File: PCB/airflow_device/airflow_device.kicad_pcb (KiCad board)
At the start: 2 copper layers, 2 parts, among them J1 GRID_EYE Connector, U1 esp32-wemos-d1-mini

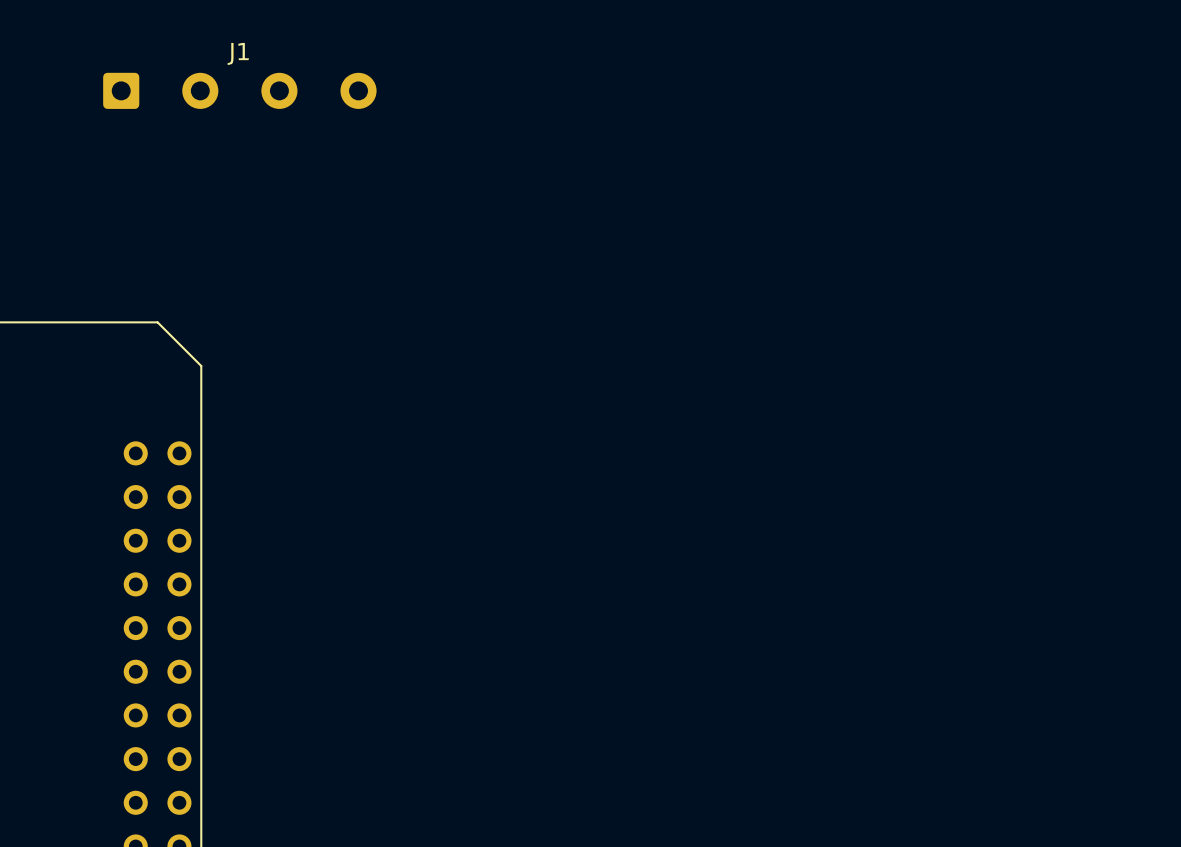
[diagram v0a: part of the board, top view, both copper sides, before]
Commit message: Adding more components, and fixing footprints
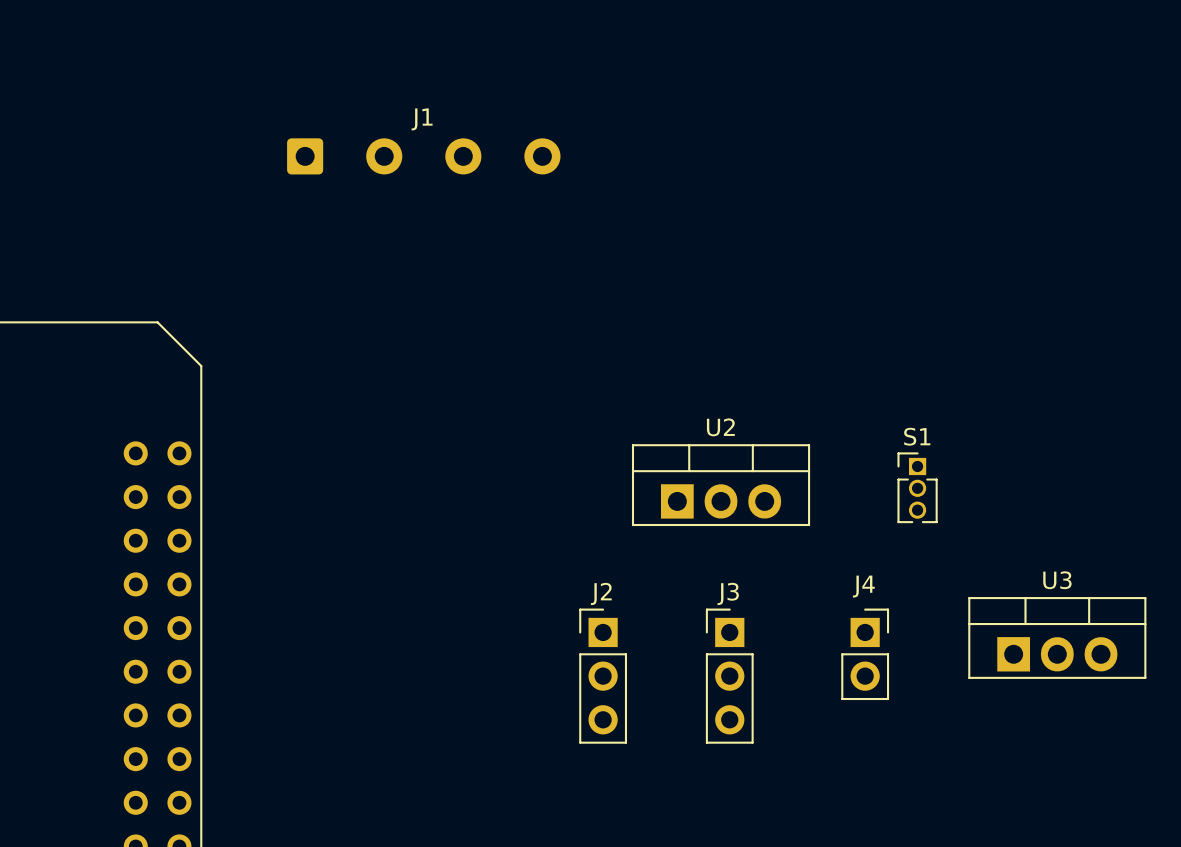
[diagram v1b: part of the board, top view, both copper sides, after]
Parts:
- added J2: Grideye Servo, Connector_PinHeader_2.54mm:PinHeader_1x03_P2.54mm_Vertical, F.Cu at (155.4, 88.9)
- added J3: Vent Servo, Connector_PinHeader_2.54mm:PinHeader_1x03_P2.54mm_Vertical, F.Cu at (162.8, 88.9)
- added J4: Conn_01x02_Pin, Connector_PinSocket_2.54mm:PinSocket_1x02_P2.54mm_Vertical, F.Cu at (170.7, 88.9)
- added S1: Toggle Switch, Connector_PinHeader_1.27mm:PinHeader_1x03_P1.27mm_Vertical, F.Cu at (173.7, 79.2)
- added U2: 3v3 regulator, Package_TO_SOT_THT:TO-220-3_Vertical, F.Cu at (159.8, 81.3)
- added U3: LM2940, Package_TO_SOT_THT:TO-220-3_Vertical, F.Cu at (179.3, 90.2)
- moved J1 11.4 mm to (138.1, 61.2)
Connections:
- J1 pad 1: unconnected-(J1-GND-Pad1) -> GND
- J1 pad 2: unconnected-(J1-SDA-Pad2) -> Net-(J1-SDA)
- J1 pad 3: unconnected-(J1-SCL-Pad3) -> Net-(J1-SCL)
- J1 pad 4: unconnected-(J1-Vin-Pad4) -> /3v3
- U1 pad 1: unconnected-(U1-GND-Pad1) -> GND
- U1 pad 16: unconnected-(U1-3V3-Pad16) -> /3v3
- U1 pad 22: unconnected-(U1-GND-Pad22) -> GND
- U1 pad 25: unconnected-(U1-IO_22/D1/SCL-Pad25) -> Net-(J1-SCL)
- U1 pad 27: unconnected-(U1-IO_21/D2/SDA-Pad27) -> Net-(J1-SDA)
- U1 pad 33: unconnected-(U1-GND-Pad33) -> GND
- U1 pad 34: unconnected-(U1-IO_00-Pad34) -> Net-(J3-SIG)
- U1 pad 36: unconnected-(U1-IO_02-Pad36) -> Net-(J2-SIG)

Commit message: Likely Functional PCB
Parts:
- removed S1: Toggle Switch, Connector_PinHeader_1.27mm:PinHeader_1x03_P1.27mm_Vertical
- added C2: 0.47uF, Capacitor_SMD:C_0805_2012Metric_Pad1.18x1.45mm_HandSolder, F.Cu at (104.6, 101.1)
- added C3: 22uF, Capacitor_SMD:C_0805_2012Metric_Pad1.18x1.45mm_HandSolder, F.Cu at (110.9, 101.1)
- added C4: .1uF, Capacitor_SMD:C_0805_2012Metric_Pad1.18x1.45mm_HandSolder, F.Cu at (95.7, 101.1)
- added C5: 10uF, Capacitor_SMD:C_0805_2012Metric_Pad1.18x1.45mm_HandSolder, F.Cu at (89.6, 101.1)
- added D1: Tracking LED, LED_THT:LED_D3.0mm, F.Cu at (85.1, 106.3)
- added D2: LED, LED_THT:LED_D3.0mm, F.Cu at (93.0, 106.3)
- added D3: LED, LED_THT:LED_D3.0mm, F.Cu at (77.0, 106.3)
- added R1: 4.7k, Resistor_SMD:R_0805_2012Metric_Pad1.20x1.40mm_HandSolder, F.Cu at (86.4, 109.6)
- added R2: 4.7k, Resistor_SMD:R_0805_2012Metric_Pad1.20x1.40mm_HandSolder, F.Cu at (100.3, 72.1)
- added R3: 4.7k, Resistor_SMD:R_0805_2012Metric_Pad1.20x1.40mm_HandSolder, F.Cu at (100.3, 77.2)
- added R4: 4.7k, Resistor_SMD:R_0805_2012Metric_Pad1.20x1.40mm_HandSolder, F.Cu at (94.0, 109.6)
- added R5: 4.7k, Resistor_SMD:R_0805_2012Metric_Pad1.20x1.40mm_HandSolder, F.Cu at (78.2, 109.6)
- added R6: 4.7k, Resistor_SMD:R_0805_2012Metric_Pad1.20x1.40mm_HandSolder, F.Cu at (78.0, 92.5)
- added R7: 4.7k, Resistor_SMD:R_0805_2012Metric_Pad1.20x1.40mm_HandSolder, F.Cu at (83.0, 79.5)
- added SW1: TOGGLE, Connector_PinHeader_2.54mm:PinHeader_1x03_P2.54mm_Vertical, F.Cu at (78.0, 96.5)
- added SW2: LEFT, Button_Switch_THT:SW_PUSH_6mm_H5mm, F.Cu at (88.4, 72.6)
- added SW3: RIGHT, Button_Switch_THT:SW_PUSH_6mm_H5mm, F.Cu at (104.5, 72.7)
- added SW4: XTRA, Button_Switch_THT:SW_PUSH_6mm_H5mm, F.Cu at (77.8, 72.2)
- J1: footprint Connector_Wire:SolderWire-0.5sqmm_1x04_P4.6mm_D0.9mm_OD2.1mm -> Connector_PinHeader_2.54mm:PinHeader_1x04_P2.54mm_Vertical
- moved U3 74.7 mm to (105.1, 98.6)
- moved U2 72.0 mm to (89.9, 98.6)
- moved J4 66.5 mm to (106.9, 107.7), turned to -90 degrees
- moved J1 24.9 mm to (147.3, 84.3), turned to 180 degrees
- moved J2 20.7 mm to (147.3, 107.9), turned to 180 degrees
- moved J3 16.6 mm to (147.3, 94.7), turned to 180 degrees
- moved U1 12.5 mm to (129.0, 92.7)
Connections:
- net Net-(J1-SCL) renamed /SCL
- net Net-(J1-SDA) renamed /SDA
- U1 pad 10: unconnected-(U1-IO_19/D6-Pad10) -> Net-(U1-IO_19/D6)
- U1 pad 12: unconnected-(U1-IO_23/D7-Pad12) -> Net-(U1-IO_23/D7)
- U1 pad 14: unconnected-(U1-IO_05/D8-Pad14) -> Net-(U1-IO_05/D8)
- U1 pad 29: unconnected-(U1-IO_17/D3-Pad29) -> Net-(U1-IO_17/D3)
- U1 pad 31: unconnected-(U1-IO_16/D4-Pad31) -> Net-(U1-IO_16/D4)
- U1 pad 6: unconnected-(U1-IO_26/D0-Pad6) -> Net-(U1-IO_26/D0)
- U1 pad 8: unconnected-(U1-IO_18/D5-Pad8) -> Net-(SW1-C)
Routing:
- net /5V: track 0.00 -> 102.4 mm
- net Net-(U1-IO_17/D3): track 0.00 -> 62.5 mm
- net Net-(SW1-C): track 0.00 -> 50.7 mm
- net Net-(U1-IO_05/D8): track 0.00 -> 50.6 mm
- net Net-(U1-IO_19/D6): track 0.00 -> 49.3 mm
- net Net-(U1-IO_16/D4): track 0.00 -> 46.1 mm
- net Net-(U1-IO_26/D0): track 0.00 -> 45.8 mm
- net Net-(U1-IO_23/D7): track 0.00 -> 45.8 mm
- net /BATT: track 0.00 -> 37.0 mm
- net GND: track 0.00 -> 14.3 mm, vias 0 -> 1
- net /SCL: track 0.00 -> 10.8 mm
- net /SDA: track 0.00 -> 10.8 mm
- net Net-(J2-SIG): track 0.00 -> 8.12 mm
- net Net-(J3-SIG): track 0.00 -> 6.12 mm
- net Net-(D2-A): track 0.00 -> 4.35 mm
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- added copper zone on F.Cu, net /3v3
- added copper zone on F.Cu, net /5V
- added copper zone on F.Cu, net /BATT
- added copper zone on B.Cu, net GND
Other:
- board outline added: 76.2 x 41.9 mm

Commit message: Added 68uF caps for servos
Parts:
- added C1: 68uF, Capacitor_THT:CP_Radial_D7.5mm_P2.50mm, F.Cu at (156.2, 96.1)
- added C6: 68uF, Capacitor_THT:CP_Radial_D7.5mm_P2.50mm, F.Cu at (156.2, 105.2)

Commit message: PCB Done
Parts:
- removed R1: 4.7k, Resistor_SMD:R_0805_2012Metric_Pad1.20x1.40mm_HandSolder
- added TP1: 3.3V, TestPoint:TestPoint_Pad_2.5x2.5mm, F.Cu at (155.2, 77.0)
- added TP2: 5V, TestPoint:TestPoint_Pad_2.5x2.5mm, F.Cu at (151.1, 98.6)
- added TP3: GND, TestPoint:TestPoint_Pad_2.5x2.5mm, F.Cu at (155.2, 82.5)
- moved C1 4.68 mm to (153.7, 92.2)
- moved C6 2.59 mm to (153.7, 105.7)
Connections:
- R6 pad 2: Net-(SW1-C) -> Net-(D1-A)
- SW1 pad 3: Net-(SW1-C) -> Net-(D1-A)
- U1 pad 12: Net-(U1-IO_23/D7) -> unconnected-(U1-IO_23/D7-Pad12)
- U1 pad 32: unconnected-(U1-IO_04-Pad32) -> Net-(J3-SIG)
- U1 pad 34: Net-(J3-SIG) -> unconnected-(U1-IO_00-Pad34)
- U1 pad 8: Net-(SW1-C) -> Net-(D1-A)
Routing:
- net Net-(D1-A): track 4.24 -> 73.8 mm
- net Net-(SW1-C): track 50.7 -> 0.00 mm
- net Net-(U1-IO_23/D7): track 45.8 -> 0.00 mm
- net /BATT: track 37.0 -> 16.5 mm
- net /5V: track 102.4 -> 95.9 mm
- net /3v3: track 0.00 -> 4.38 mm
- net Net-(J3-SIG): track 6.12 -> 5.06 mm
- net GND: vias 1 -> 2
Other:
- board size 76.2 x 41.9 mm -> 84.6 x 42.7 mm
- board text added: "3.3V"
- board text added: "GND"
- board text added: "SCL"
- board text added: "SDA"
